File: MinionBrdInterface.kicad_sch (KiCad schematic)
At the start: 4 parts, among them J30 Backup Camera, J5 MinionConn, J6 SPI, SW1 BACKUP_SW

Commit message: Remove 12V isolator, swap CAN connector pins, etc.
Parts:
- SW1: footprint UTSVT_Special:2M1-SP1-T1-B1-M2QE -> (none)
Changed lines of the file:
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@@
     (effects (font (size 1.27 1.27)) (justify left))
   )
-  (symbol (lib_id "Connector_Generic:Conn_02x05_Top_Bottom") (at 118.11 100.33 0)
+  (symbol (lib_id "Connector_Generic:Conn_02x05_Top_Bottom") (at 118.11 100.33 0) (unit 1)
     (in_bom yes) (on_board yes)
     (property "Reference" "J5" (id 0) (at 118.11 110.49 0)
@@
     (property "Reference" "SW1" (id 0) (at 208.28 93.091 0))
     (property "Value" "BACKUP_SW" (id 1) (at 208.28 95.4024 0))
-    (property "Footprint" "UTSVT_Special:2M1-SP1-T1-B1-M2QE" (id 2) (at 208.28 100.33 0)
+    (property "Footprint" "" (id 2) (at 208.28 100.33 0)
       (effects (font (size 1.27 1.27)) hide)
     )

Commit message: Release v2.4 and gerbers
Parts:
- SW1: footprint (none) -> Connector_Molex:Molex_Micro-Fit_3.0_43650-0315_1x03_P3.00mm_Vertical
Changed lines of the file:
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@@
     (property "Reference" "SW1" (id 0) (at 208.28 93.091 0))
     (property "Value" "BACKUP_SW" (id 1) (at 208.28 95.4024 0))
-    (property "Footprint" "" (id 2) (at 208.28 100.33 0)
+    (property "Footprint" "Connector_Molex:Molex_Micro-Fit_3.0_43650-0315_1x03_P3.00mm_Vertical" (id 2) (at 208.28 100.33 0)
       (effects (font (size 1.27 1.27)) hide)
     )

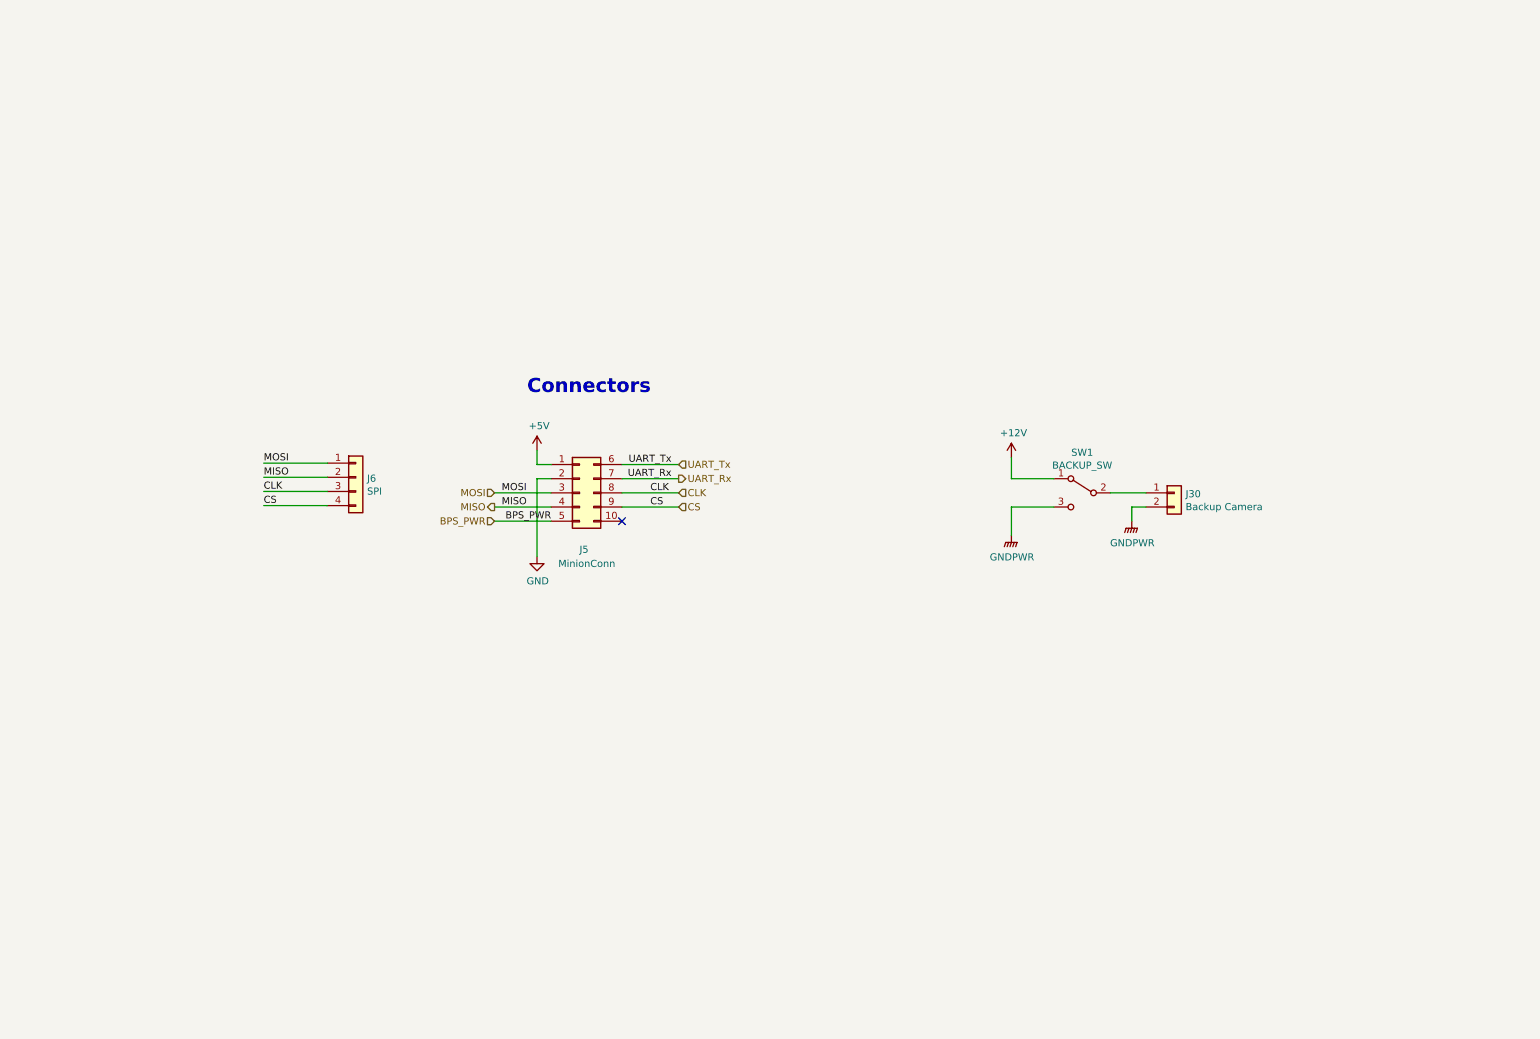
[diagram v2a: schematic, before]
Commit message: Daybreak rework (#24)
* Schematic notations for rework changes

* Updated schematic in accordance to previous weeks annotated changes

* Added .lck files to .gitignore.

* Renamed Clk to PA5, removed CAN_TX/RX test points, deleted other .lck file and #auto_saved_files# (hopefully this does not break anything.

* Changed testpoints to pin headers.

* removed camera, fixed connectors, and changed status LEDS

* Schematic finished :) hopefully not broken

* Added back lights + drivers + timer for all blinkers and brake lights

* Fuse added for motorCAN 12V

* Renamed local net labels to be different from hierarchical ones in the MinionBrdInterface so that they aren't connected. Changed Regen input to BPS Hazard light since we aren't using regen but will be alerting the driver of BPS faults.

* Flipped optoisolators, changed resistor values, added second connector to motor can and disconnected shield pins for now since I haven't seen them used (will chack against old version to see what the circuit looked like), copied power-in circuit from contactor board, added optoisolator to timer and blinker light connection.

* Changed names and added power flags until KiCAD ERC was satisfied. Hopefully this did not involve doing anything that wasn't supposed to be done.

* Added UTSVT libraries to the gitignore.

* Added footprints. I think this is everything except the fuse.

* Fuse footprint added and blinker changed to software

* Started cleaning some comments, changed EL3H7 data sheet link, removed extra motor CAN connector and changed original one to match (I think) motor controller connector, removed extra mounting holes, removed hierarchical power labels.

* renamed power state indicators to contactors and removed unused contactors, added current limiting resistors to lights drivers, changed mosfet to new mosfet

* Updated contactor pins.

* added circuitry for limit switch brake, added mosfet to drive LEDs, cleaned up legacy comments, 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
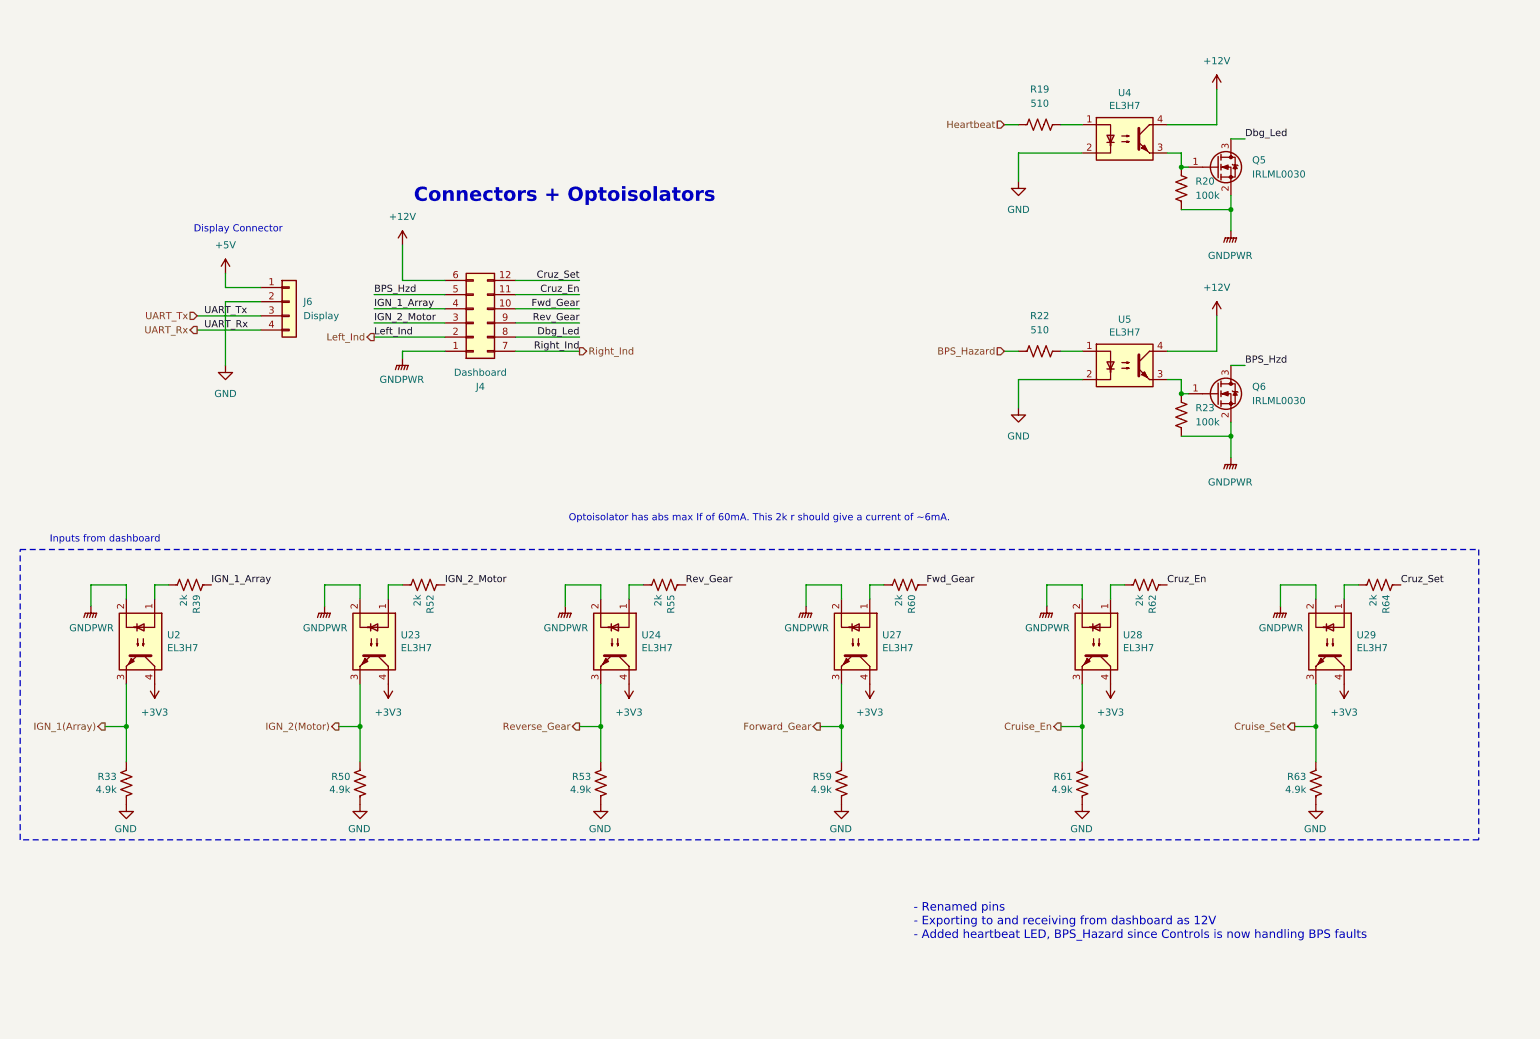
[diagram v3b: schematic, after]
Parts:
- removed J30: Backup Camera, Connector_Molex:Molex_Micro-Fit_3.0_43650-0215_1x02_P3.00mm_Vertical, symbol Connector_Generic:Conn_01x02
- removed J5: MinionConn, Connector_Molex:Molex_Micro-Fit_3.0_43045-1012_2x05_P3.00mm_Vertical, symbol Connector_Generic:Conn_02x05_Top_Bottom
- removed SW1: BACKUP_SW, Connector_Molex:Molex_Micro-Fit_3.0_43650-0315_1x03_P3.00mm_Vertical, symbol Switch:SW_SPDT
- added J4: Dashboard, UTSVT_Connectors:Molex_MicroFit3.0_2x6xP3.00mm_PolarizingPeg_Vertical, symbol Connector_Generic:Conn_02x06_Top_Bottom
- added Q5, Q6: IRLML0030, Package_TO_SOT_SMD:SOT-23, symbol Transistor_FET:IRLML0030
- added R19, R22: 510, Resistor_SMD:R_0805_2012Metric, symbol Device:R_US
- added R20, R23: 100k, Resistor_SMD:R_0805_2012Metric, symbol Device:R_US
- added R33, R50, R53, R59, R61, R63: 4.9k, Resistor_SMD:R_0805_2012Metric, symbol Device:R_US
- added R39, R52, R55, R60, R62, R64: 2k, Resistor_SMD:R_0805_2012Metric, symbol Device:R_US
- added U2, U23, U24, U27, U28, U29, U4, U5: EL3H7, Package_SO:SSOP-4_4.4x2.6mm_P1.27mm, symbol Isolator:SFH617A-1
- J6: value SPI -> Display; footprint Connector_PinHeader_2.54mm:PinHeader_1x04_P2.54mm_Vertical -> Connector_Molex:Molex_Micro-Fit_3.0_43650-0415_1x04_P3.00mm_Vertical; P/N (none) -> 436500244
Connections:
- net CLK is gone; now on net UART_Tx: J6.3 (Pin_3)
- net CS is gone; now on net UART_Rx: J6.4 (Pin_4)
- net MISO is gone; now on net GND: J6.2 (Pin_2)
- net MOSI is gone; now on net +5V: J6.1 (Pin_1)
- net +12V: now also J4.6 (Pin_6), U4.4, U5.4
- net GND: now also R33.2, R50.2, R53.2, R59.2, R61.2, R63.2, U4.2, U5.2
- net GNDPWR: now also J4.1 (Pin_1), Q5.2 (S), Q6.2 (S), R20.2, R23.2, U2.2, U23.2, U24.2, U27.2, U28.2, U29.2
- new net: R22.2, U5.1
- new net: Q6.1 (G), R23.1, U5.3
- new net: R60.2, U27.1
- new net: R55.2, U24.1
- new net: R19.2, U4.1
- new net: Q5.1 (G), R20.1, U4.3
- new net: R64.2, U29.1
- new net: R39.2, U2.1
- new net: R52.2, U23.1
- new net: R62.2, U28.1
- new net +3V3: U2.4, U23.4, U24.4, U27.4, U28.4, U29.4
- new net BPS_Hazard: R22.1
- new net BPS_Hzd: J4.5 (Pin_5), Q6.3 (D)
- new net Cruise_En: R61.1, U28.3
- new net Cruise_Set: R63.1, U29.3
- new net Cruz_En: J4.11 (Pin_11), R62.1
- new net Cruz_Set: J4.12 (Pin_12), R64.1
- new net Dbg_Led: J4.8 (Pin_8), Q5.3 (D)
- new net Forward_Gear: R59.1, U27.3
- new net Fwd_Gear: J4.10 (Pin_10), R60.1
- new net Heartbeat: R19.1
- new net IGN_1(Array): R33.1, U2.3
- new net IGN_1_Array: J4.4 (Pin_4), R39.1
- new net IGN_2(Motor): R50.1, U23.3
- new net IGN_2_Motor: J4.3 (Pin_3), R52.1
- new net Left_Ind: J4.2 (Pin_2)
- new net Rev_Gear: J4.9 (Pin_9), R55.1
- new net Reverse_Gear: R53.1, U24.3
- new net Right_Ind: J4.7 (Pin_7)
- no-connect marks 1 -> 0
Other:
- note added: "- Renamed pins - Exporting to and receiving from dashboard as 12V - Added heartbeat LED, BPS_Hazard since Controls is now handling BPS faults"
- note added: "Connectors + Optoisolators"
- note added: "Display Connector"
- note added: "Inputs from dashboard"
- note added: "Optoisolator has abs max If of 60mA. This 2k r should give a current of ~6mA."
- note removed: "Connectors"

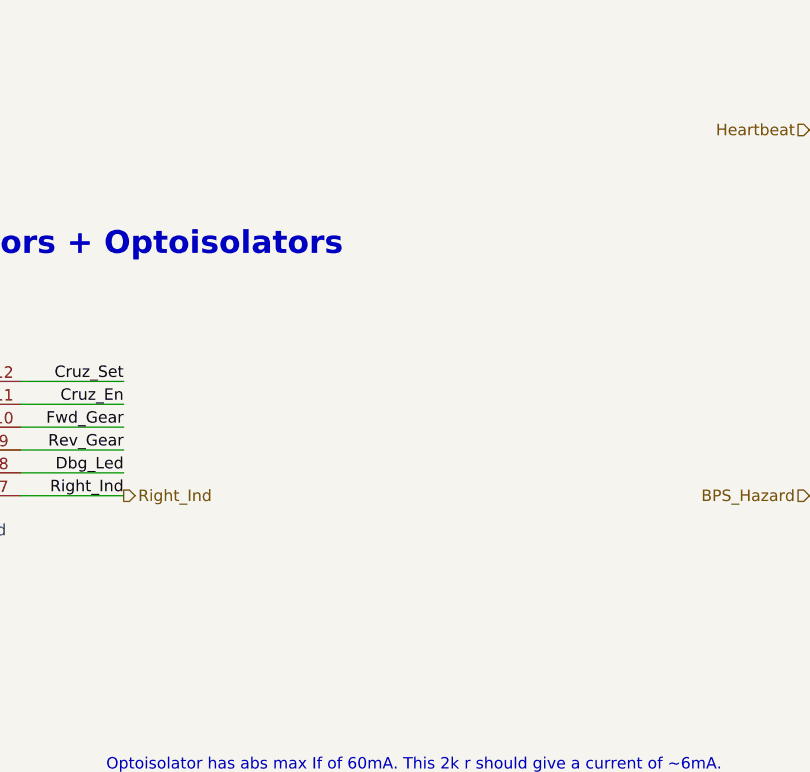
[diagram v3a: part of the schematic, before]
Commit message: Changed lights to direct drive instead of timer_CLK optoisolator stuff.
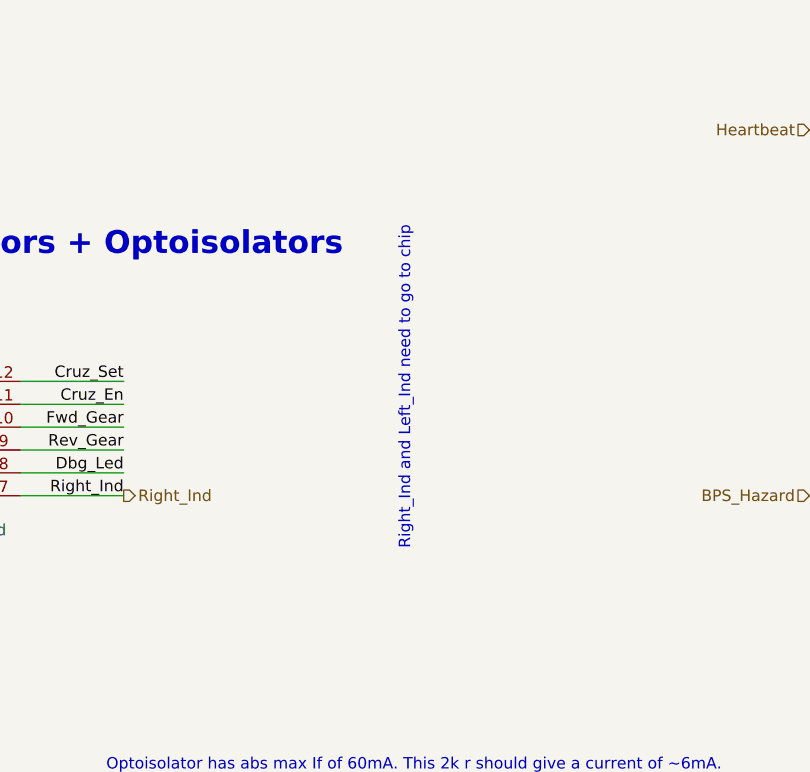
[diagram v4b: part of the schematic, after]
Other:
- note added: "Right_Ind and Left_Ind need to go to chip"
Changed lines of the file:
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@@
+		)
+	)
+	(text "Right_Ind and Left_Ind need to go to chip"
+		(exclude_from_sim no)
+		(at 149.352 62.992 90)
+		(effects
+			(font
+				(size 1.27 1.27)
+				(color 255 53 39 1)
+			)
 		)
 	)
